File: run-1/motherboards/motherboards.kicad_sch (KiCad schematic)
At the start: 6 parts, among them J101 Conn_01x35, J102 Conn_02x35_Counter_Clockwise, J103 Conn_01x35, J104 Conn_01x35, J105 Conn_02x35_Counter_Clockwise, J106 Conn_01x35

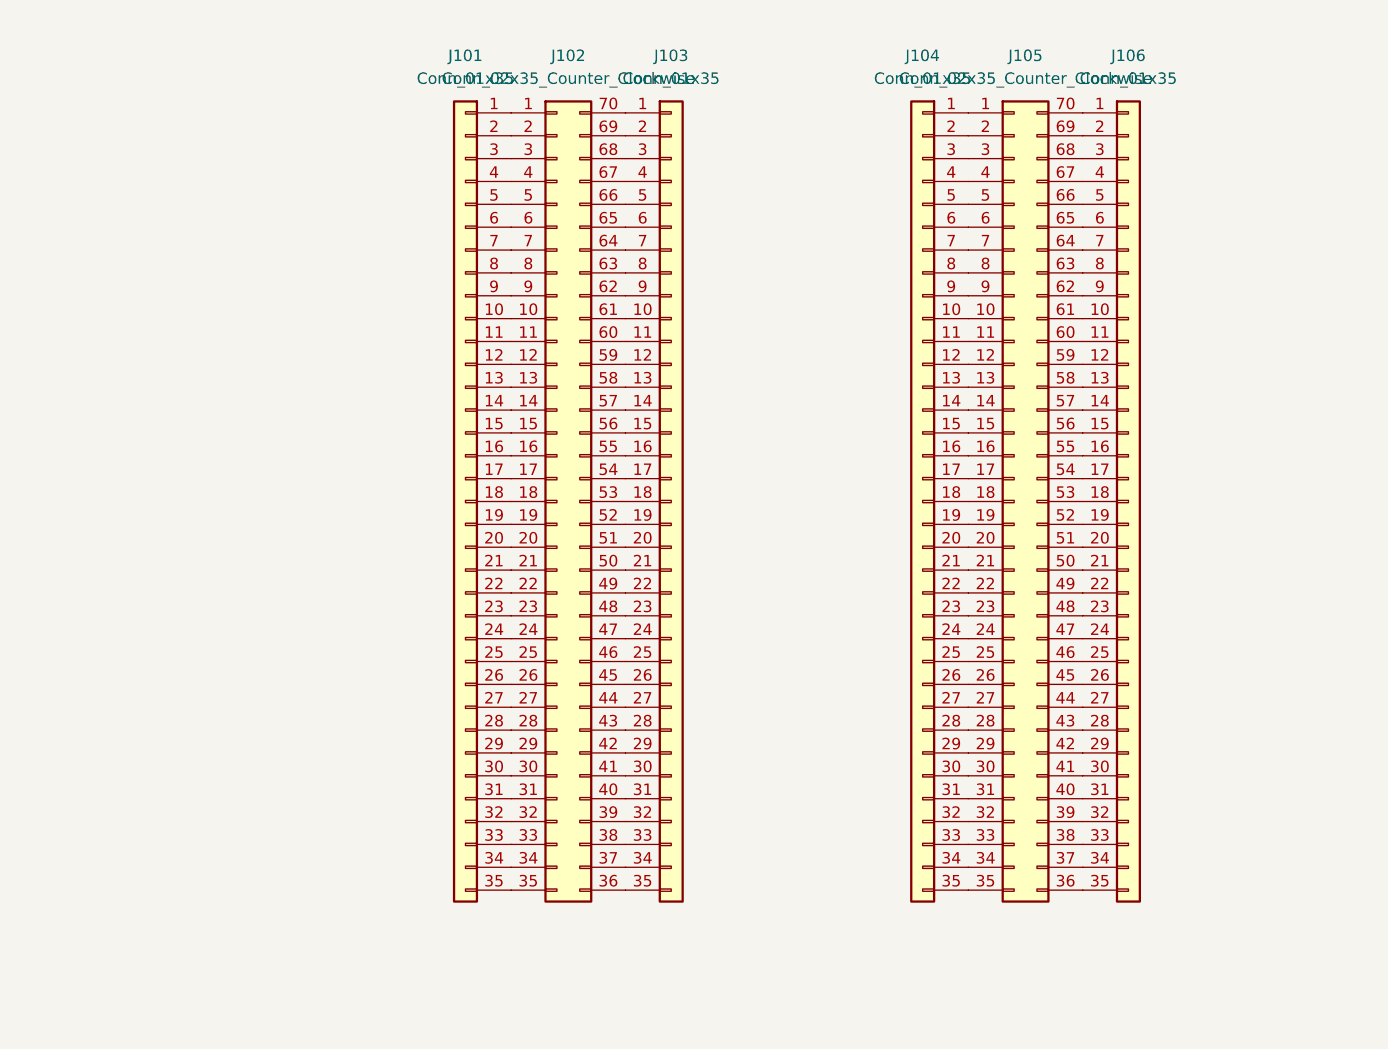
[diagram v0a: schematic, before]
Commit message: update motherboards with new symbols
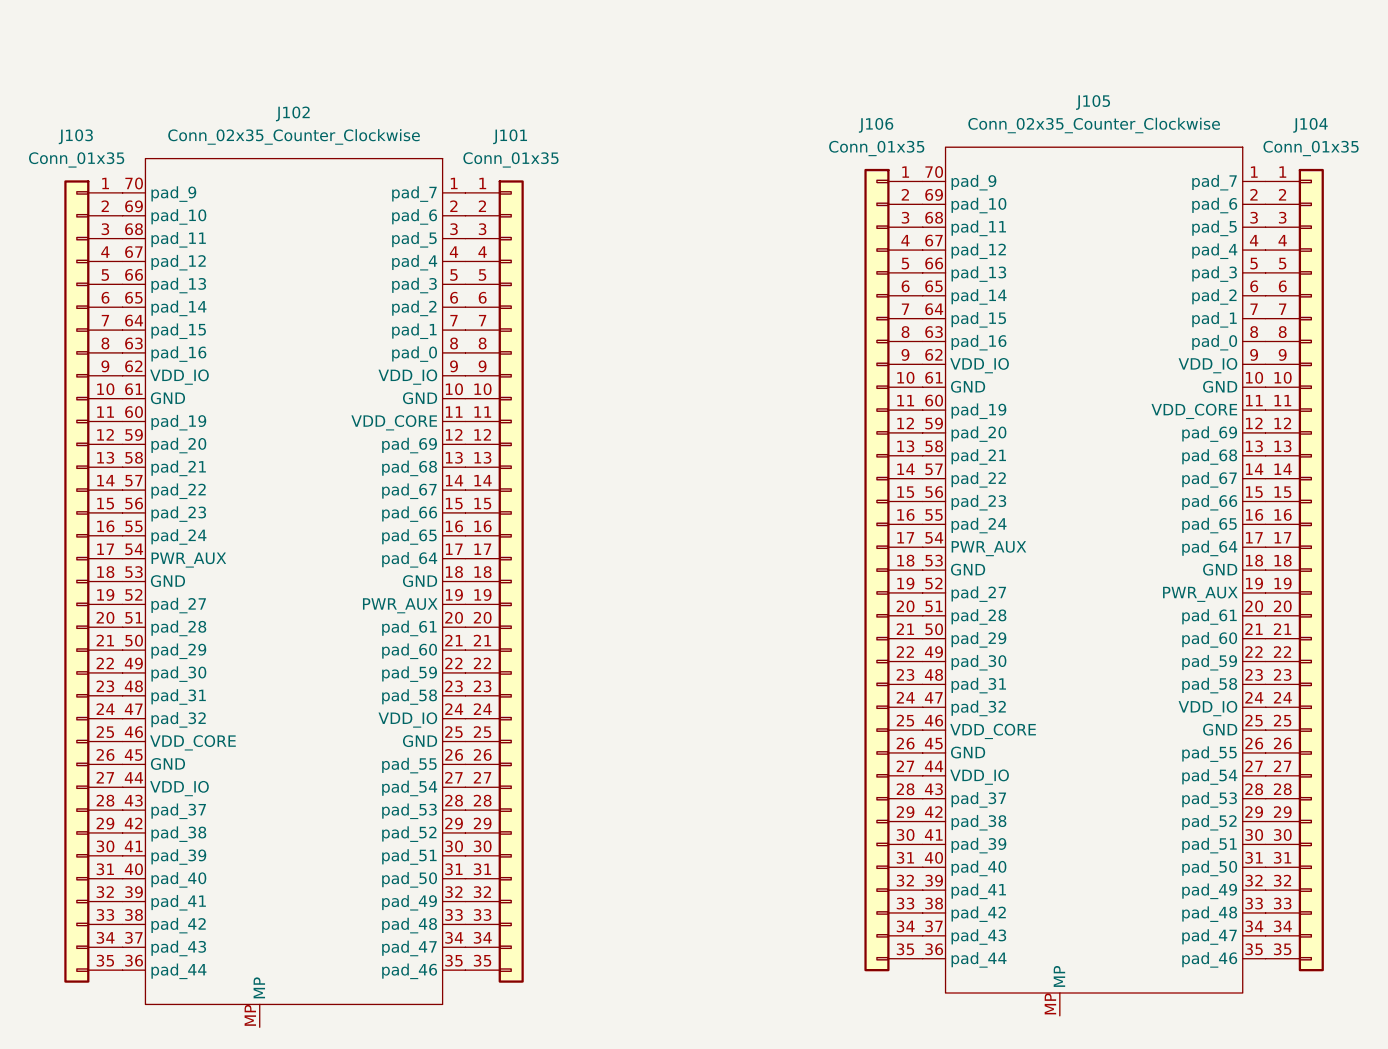
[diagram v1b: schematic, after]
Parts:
- J102, J105: footprint Connector_Mezzanine:CONN-SMD_70P-P0.40_HC-PBB40C-70DS-0.4V-3.0-02 -> Connector_Mezzanine:CONN-SMD_70P-P0.40_HCTL_HC-PBB40C-70DP-0.4V-02; symbol Connector_Generic:Conn_02x35_Counter_Clockwise -> WaferSpace:70pin_ws_default_mezzanine
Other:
- moved on the sheet: J101, J103, J104, J106

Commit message: update readmes
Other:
- note added: ".1" Header"
- note added: "Castellated"
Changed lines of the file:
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@@
+		)
+	)
+	(text "Castellated"
+		(exclude_from_sim no)
+		(at 143.51 39.37 0)
+		(effects
+			(font
+				(size 3.81 3.81)
+			)
+		)
+	)
+	(text ".1\" Header"
+		(exclude_from_sim no)
+		(at 53.34 39.37 0)
+		(effects
+			(font
+				(size 3.81 3.81)
+			)
 		)
 	)

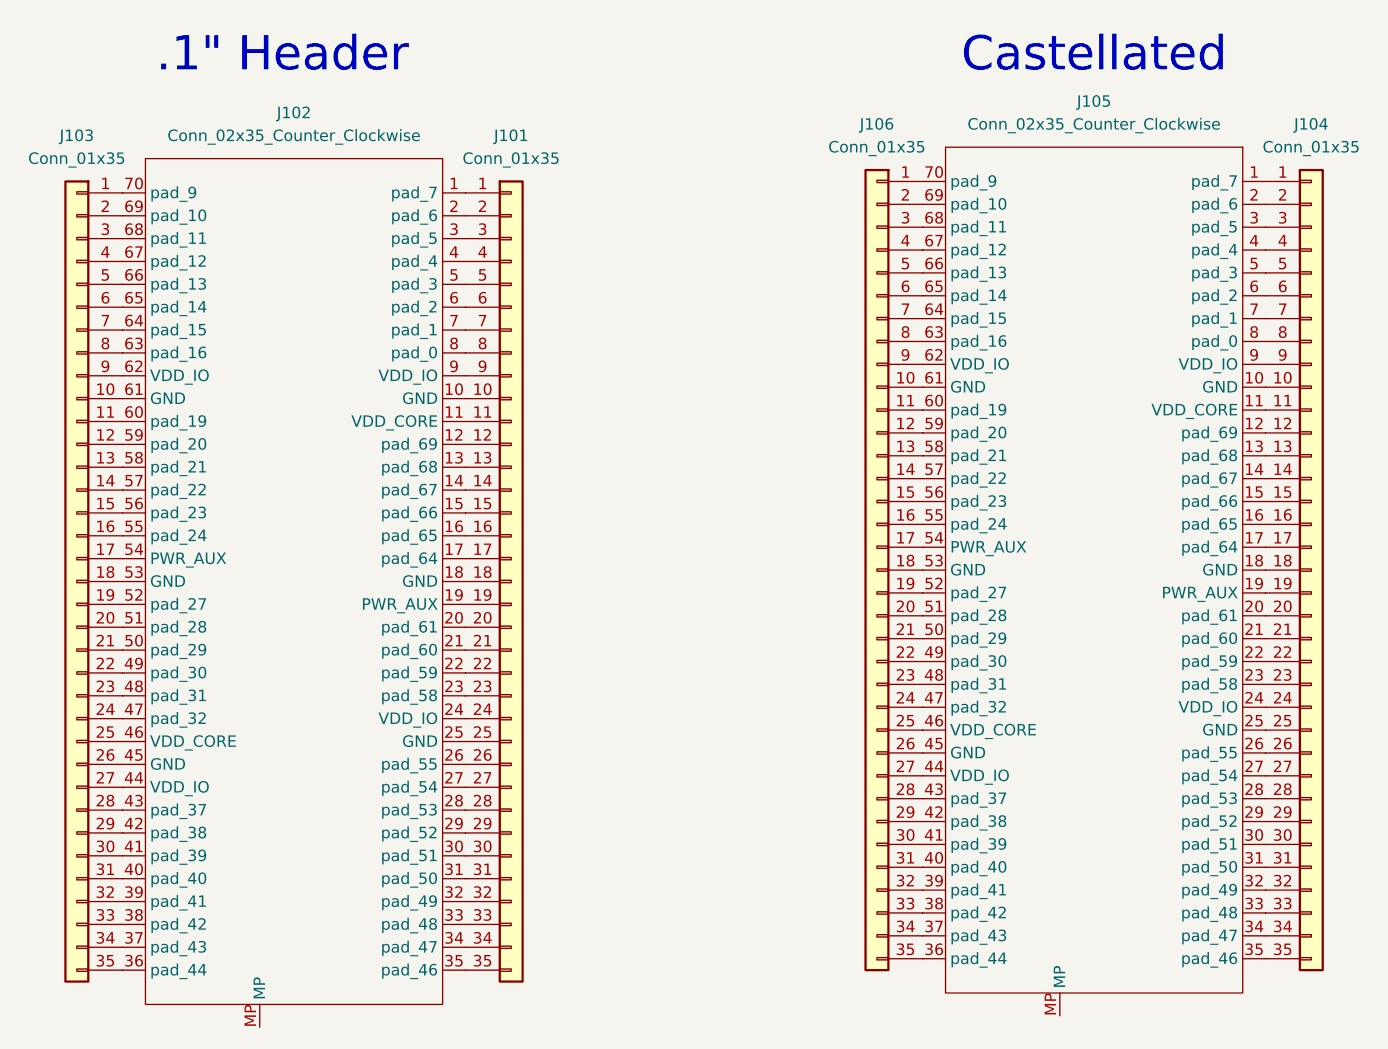
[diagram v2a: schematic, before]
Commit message: harmonize maotherboard pin naming
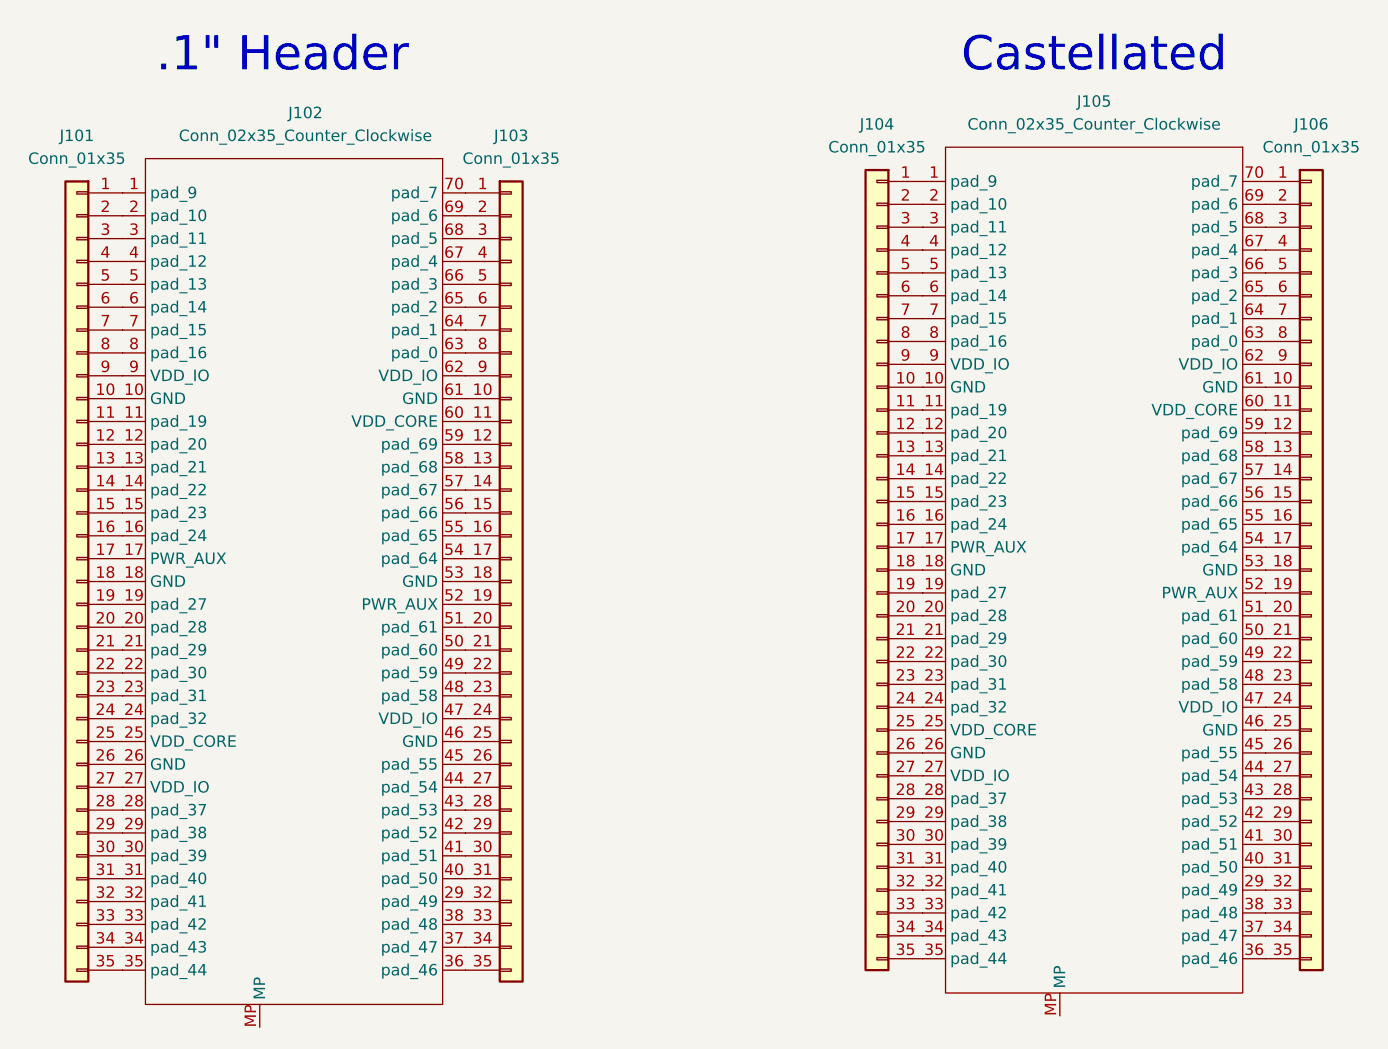
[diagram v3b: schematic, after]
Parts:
- J102, J105: symbol WaferSpace:70pin_ws_default_mezzanine -> WaferSpace:70pin_ws_default_mezzanine_motherboard
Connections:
- net at J103.32 (Pin_32): now also J102.29 (pad_49); no longer J102.39 (pad_41)
- net at J106.32 (Pin_32): now also J105.29 (pad_49); no longer J105.39 (pad_41)
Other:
- moved on the sheet: J101, J103, J104, J106

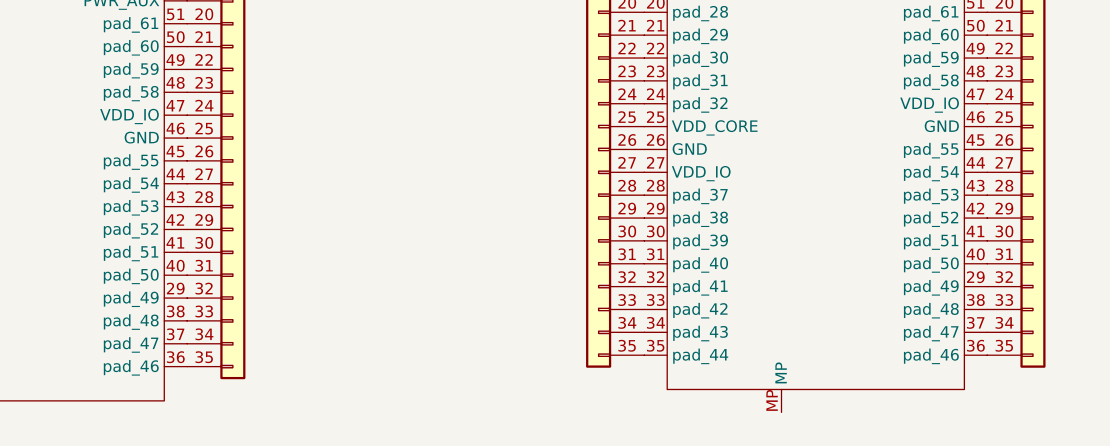
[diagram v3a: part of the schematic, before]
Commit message: fix pin numbering on motherboards
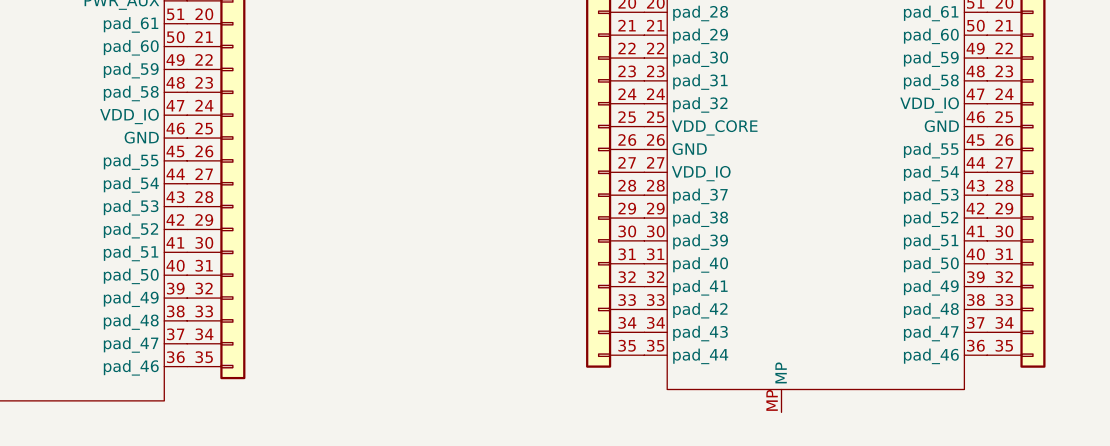
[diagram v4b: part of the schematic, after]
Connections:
- net at J102.29 (pad_38): now also J101.29 (Pin_29); no longer J103.32 (Pin_32)
- net at J106.32 (Pin_32): now also J105.39 (pad_49); no longer J105.29 (pad_49)
- new net: J102.39 (pad_49), J103.32 (Pin_32)
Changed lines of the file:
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@@
 		(pin "46"
 		)
-		(pin "29"
+		(pin "39"
 		)
 		(pin "38"
@@
 	)
 	(symbol
-		(lib_name "70pin_ws_default_mezzanine_motherboard_1")
 		(lib_id "WaferSpace:70pin_ws_default_mezzanine_motherboard")
 		(at 144.78 96.52 0)
@@
 		(pin "46"
 		)
-		(pin "29"
+		(pin "39"
 		)
 		(pin "38"
